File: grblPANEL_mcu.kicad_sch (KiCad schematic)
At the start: 28 parts, among them J201 2x5x1.27mm, J202 USB_C_Receptacle_USB2.0, SW201 SW_Push, SW202 SW_Push, U201 STM32G0B1CxTxN, U202 USBLC6-2SC6, Y201 8MHz

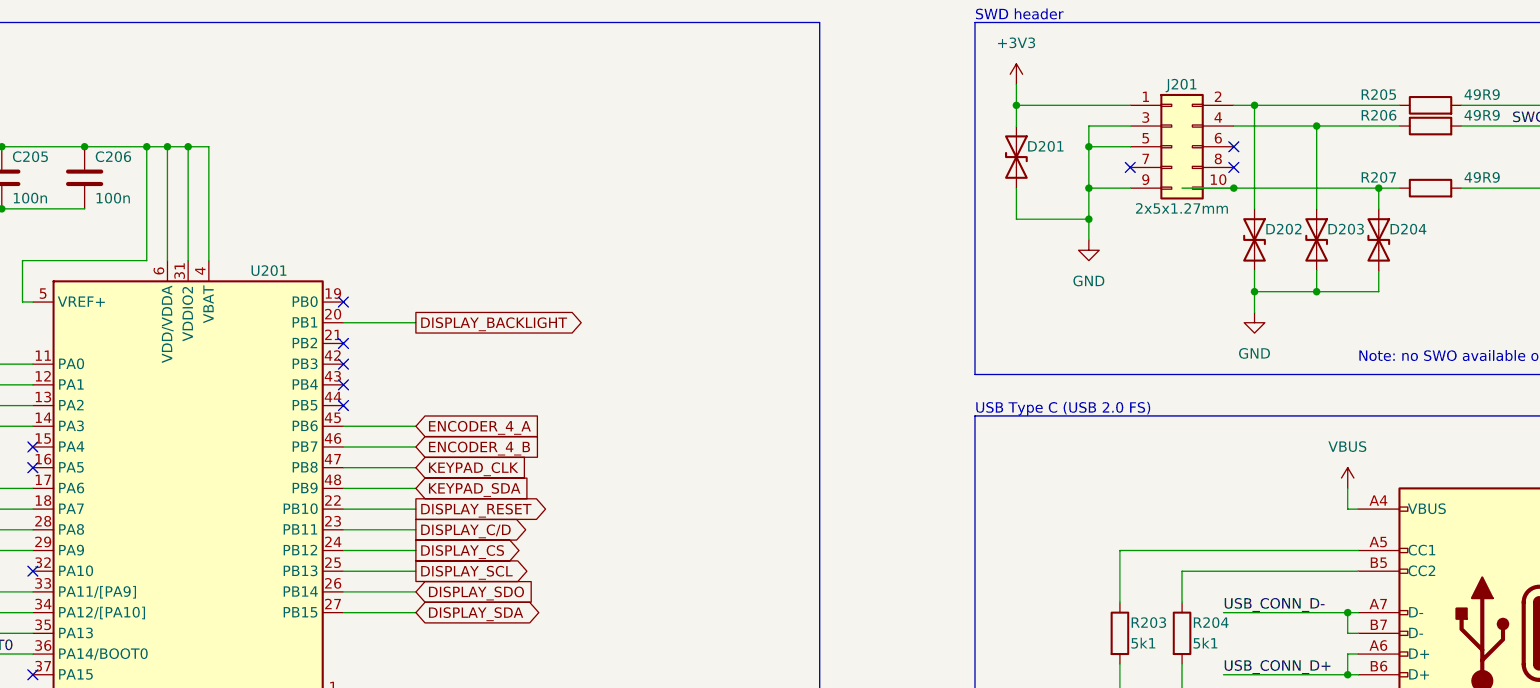
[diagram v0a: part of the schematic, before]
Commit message: ERC fixes
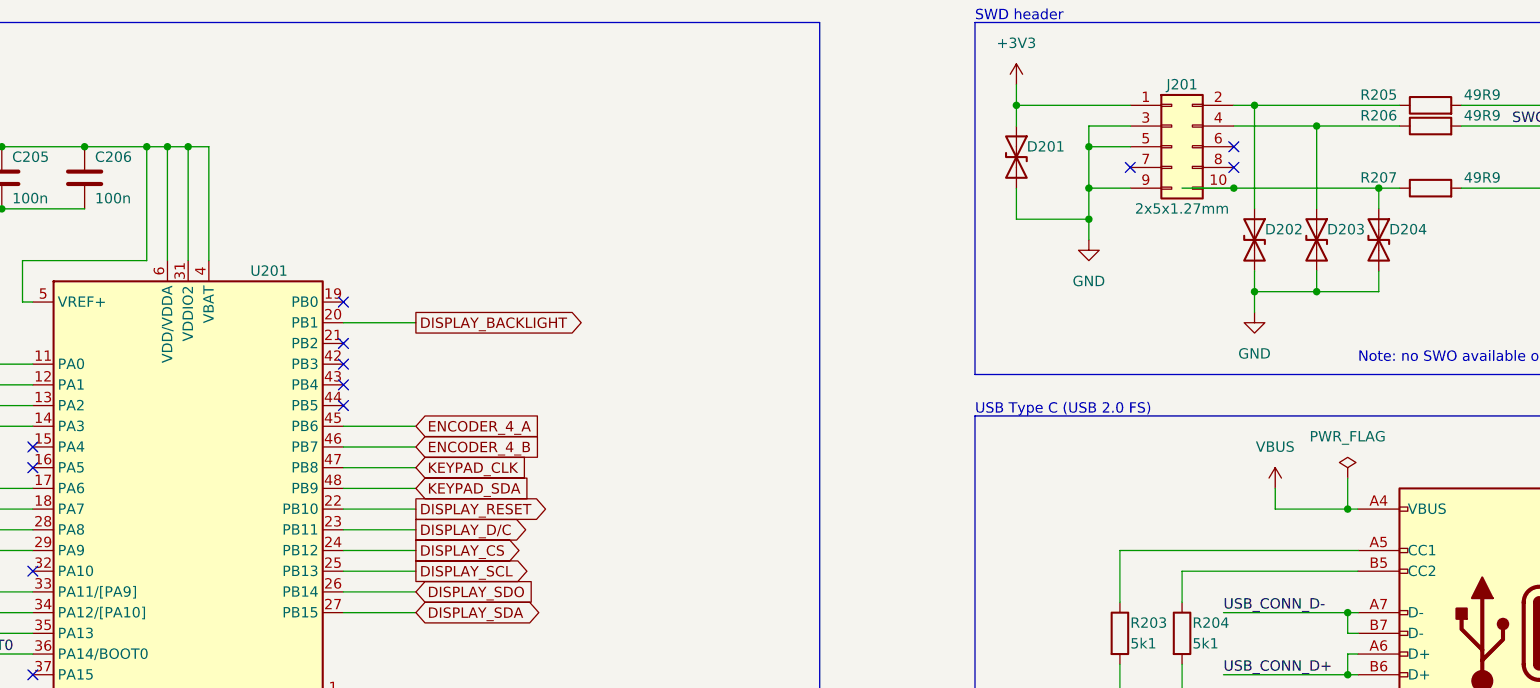
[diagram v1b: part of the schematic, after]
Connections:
- net DISPLAY_C/D renamed DISPLAY_D/C

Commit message: Refresh
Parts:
- removed C202: 1u, symbol Device:C
- removed C203, C206: 100n, symbol Device:C
- added C204: 100n, Capacitor_SMD:C_0603_1608Metric, symbol Device:C
- added R201, R203, R204: 0, Resistor_SMD:R_0603_1608Metric, symbol Device:R
- C201: footprint (none) -> Capacitor_SMD:C_0805_2012Metric
- C202: renamed from C204; footprint (none) -> Capacitor_SMD:C_0603_1608Metric
- C203: renamed from C205; footprint (none) -> Capacitor_SMD:C_0603_1608Metric
- C205: renamed from C207; footprint (none) -> Capacitor_SMD:C_0603_1608Metric
- C206: renamed from C208; footprint (none) -> Capacitor_SMD:C_0603_1608Metric
- C207: renamed from C209; footprint (none) -> Capacitor_SMD:C_0603_1608Metric
- C208: renamed from C210; footprint (none) -> Capacitor_SMD:C_0603_1608Metric
- D201, D202, D203, D204: footprint (none) -> Diode_SMD:D_SOD-323
- J201: footprint (none) -> dresco:FTSH-105-01-L-DV-K
- J202: footprint (none) -> Connector_USB:USB_C_Receptacle_HRO_TYPE-C-31-M-12
- R202: renamed from R201; value 300 -> 200; footprint (none) -> Resistor_SMD:R_0603_1608Metric
- R205: renamed from R202; footprint (none) -> Resistor_SMD:R_0603_1608Metric
- R206: renamed from R203; footprint (none) -> Resistor_SMD:R_0603_1608Metric
- R207: renamed from R204; footprint (none) -> Resistor_SMD:R_0603_1608Metric
- R208: renamed from R205; footprint (none) -> Resistor_SMD:R_0603_1608Metric
- R209: renamed from R206; footprint (none) -> Resistor_SMD:R_0603_1608Metric
- R210: renamed from R207; footprint (none) -> Resistor_SMD:R_0603_1608Metric
- SW201, SW202: footprint (none) -> Connector_Pin:Pin_D1.0mm_L10.0mm_LooseFit
- Y201: footprint (none) -> Crystal:Crystal_SMD_3225-4Pin_3.2x2.5mm
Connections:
- net +3V3: now also R204.2; no longer U201.31 (VDDIO2), U201.5 (VREF+)
- net GND: now also C204.2, R201.1, R203.2; no longer U201.30 (VSS)
- new net: C204.1, R204.1, U201.31 (VDDIO2)
- new net: R203.1, U201.30 (VSS)
- new net: R201.2, U201.5 (VREF+)
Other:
- note added: "Note: May source either STM32G0B1CET (general purpose) or STM32G0B1CETxN (power delivery) MCU parts, depending on availability. Note the following difference in pinouts; Pin GP PD 30 PC6 VSS 31 PC7 VDDIO2 Optional connection to power rails through 0 ohm resistors."
- note removed: "Note: May source either STM32G0B1CET (general purpose) or STM32G0B1CETxN (power delivery) MCU parts, depending on availability. Note the following difference in pinouts; Pin GP PD 30 PC6 VSS 31 PC7 VDDIO2 Either produce PD specific board rev, or connect to power rails through 0 ohm resistors?"
- moved on the sheet: C201, C202, C203, D203, D204

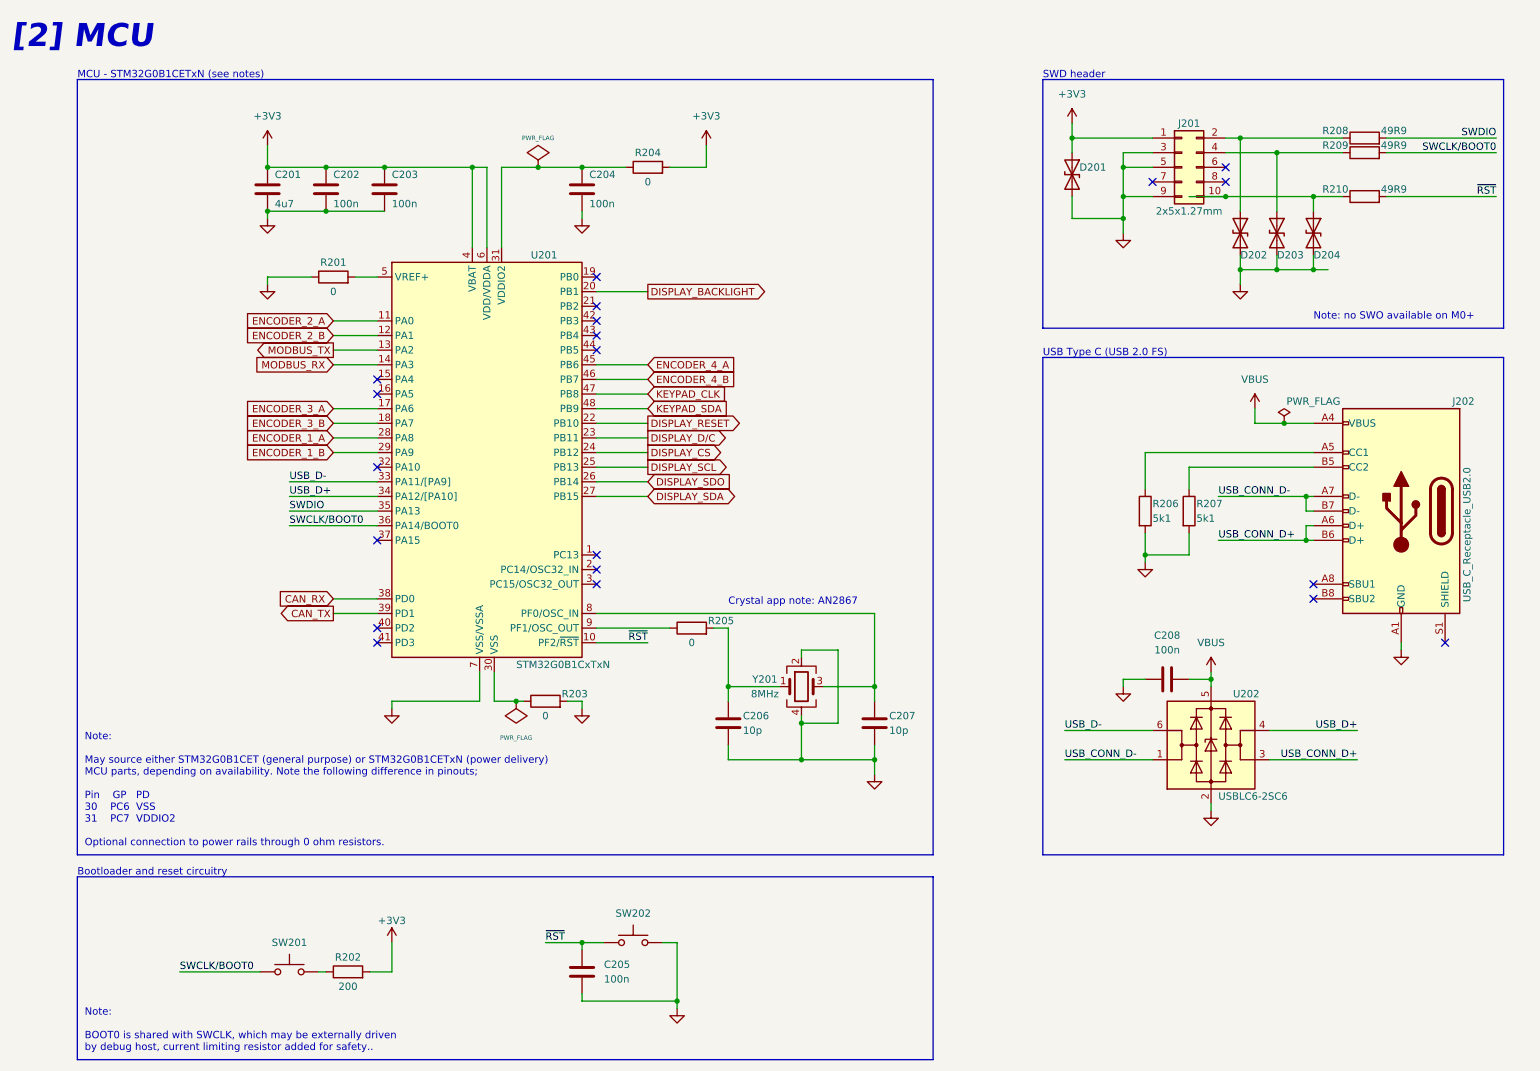
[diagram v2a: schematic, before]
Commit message: Status LED & annotation cleanup
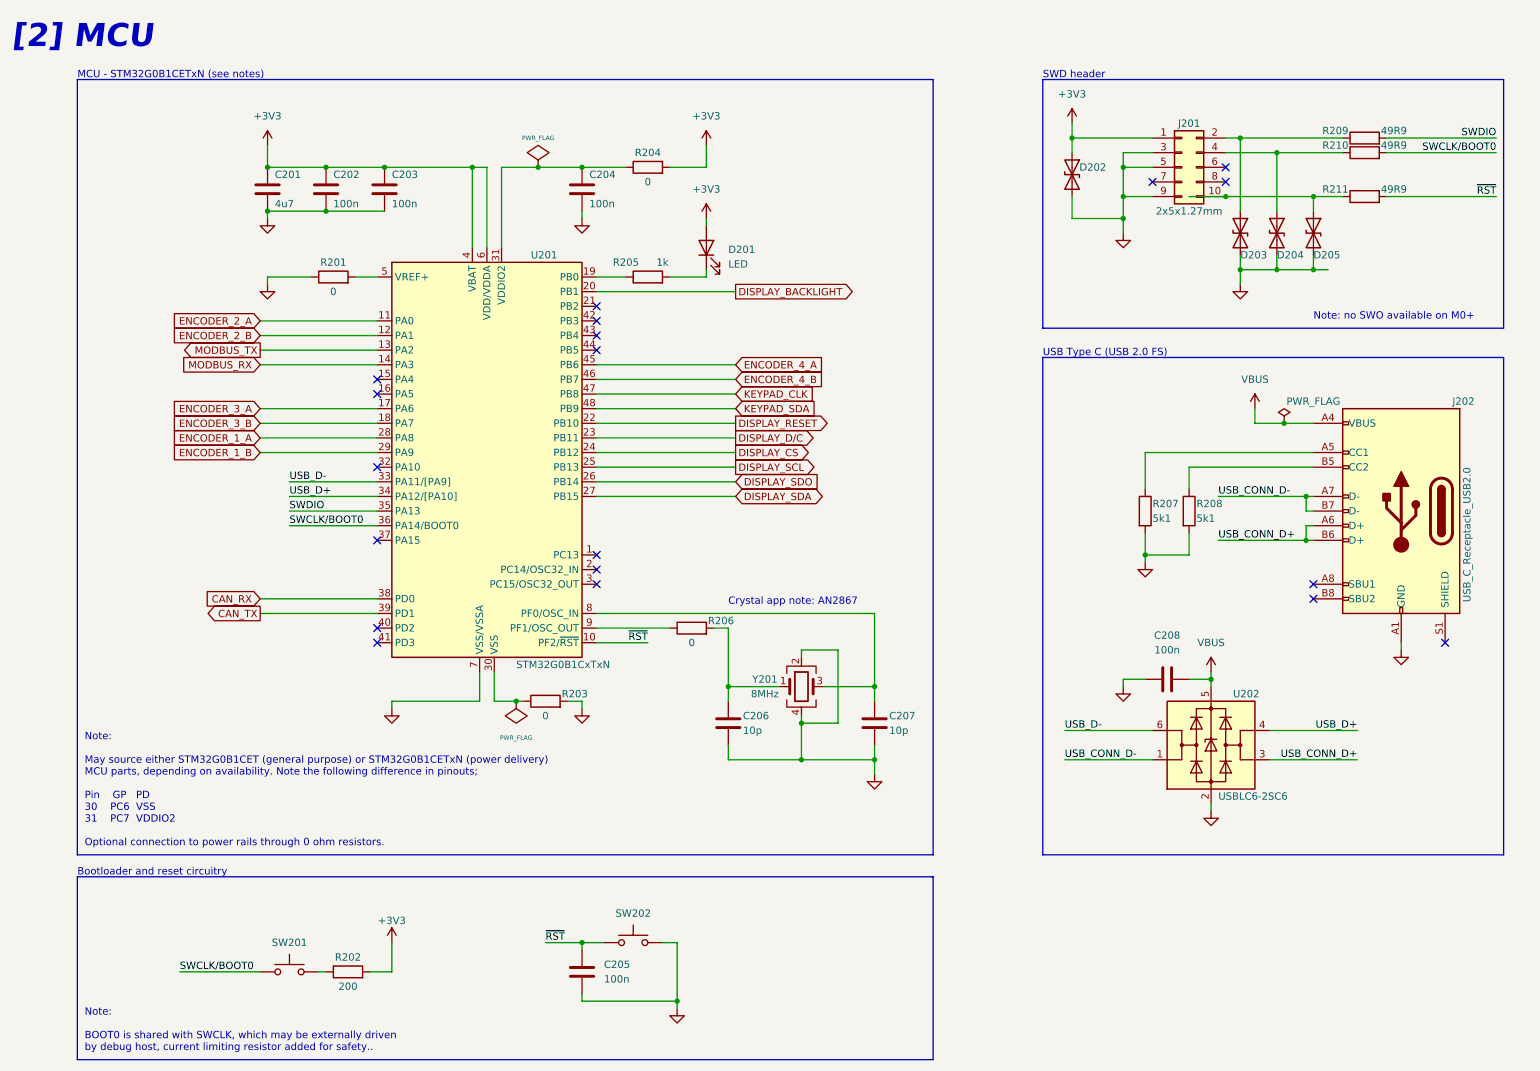
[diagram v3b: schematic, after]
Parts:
- added D201: LED, LED_SMD:LED_0603_1608Metric, symbol Device:LED
- added R205: 1k, Resistor_SMD:R_0603_1608Metric, symbol Device:R
- renumbered D201 to D202, D202 to D203, D203 to D204, D204 to D205, R205 to R206, R206 to R207, R207 to R208, R208 to R209, R209 to R210, R210 to R211
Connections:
- net +3V3: now also D201.2 (A)
- net at U201.19 (PB0): now also R205.1
- new net: D201.1 (K), R205.2
- no-connect marks 20 -> 19

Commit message: Weeny schematic update
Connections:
- net USB_CONN_CC1: now reaches J202.A5 (CC1), R207.1
- net USB_CONN_CC2: now reaches J202.B5 (CC2), R208.1
- net HSE_IN: now reaches C207.1, U201.8 (PF0/OSC_IN), Y201.3
- net XTAL_IN: now reaches C206.1, R206.2, Y201.1
- net HSE_OUT: now reaches R206.1, U201.9 (PF1/OSC_OUT)
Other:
- note added: "Cl1=Cl2=2*(C0-Cs)"
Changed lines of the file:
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@@
+    (effects (font (size 1.27 1.27)) (justify left bottom))
+  )
+  (text "Cl1=Cl2=2*(C0-Cs)" (at 142.24 147.32 0)
     (effects (font (size 1.27 1.27)) (justify left bottom))
   )
@@
     (effects (font (size 1.27 1.27)) (justify right bottom))
   )
+  (label "XTAL_IN" (at 139.7 132.08 0)
+    (effects (font (size 1.27 1.27)) (justify left bottom))
+  )
   (label "USB_D-" (at 63.5 96.52 0)
     (effects (font (size 1.27 1.27)) (justify left bottom))
   )
+  (label "HSE_IN" (at 125.73 119.38 180)
+    (effects (font (size 1.27 1.27)) (justify right bottom))
+  )
   (label "USB_CONN_D-" (at 224.79 99.06 0)
     (effects (font (size 1.27 1.27)) (justify left bottom))
   )
+  (label "USB_CONN_CC2" (at 224.79 93.98 0)
+    (effects (font (size 1.27 1.27)) (justify left bottom))
+  )
   (label "USB_CONN_D+" (at 248.92 144.78 180)
     (effects (font (size 1.27 1.27)) (justify right bottom))
@@
     (effects (font (size 1.27 1.27)) (justify left bottom))
   )
+  (label "USB_CONN_CC1" (at 224.79 91.44 0)
+    (effects (font (size 1.27 1.27)) (justify left bottom))
+  )
   (label "USB_CONN_D-" (at 198.12 144.78 0)
     (effects (font (size 1.27 1.27)) (justify left bottom))
@@
   (label "SWCLK{slash}BOOT0" (at 44.45 181.61 0)
     (effects (font (size 1.27 1.27)) (justify left bottom))
+  )
+  (label "HSE_OUT" (at 125.73 121.92 180)
+    (effects (font (size 1.27 1.27)) (justify right bottom))
   )
   (label "~{RST}" (at 273.05 46.99 180)
@@
   (symbol (lib_id "Device:Crystal_GND24") (at 152.4 132.08 0) (unit 1)
     (in_bom yes) (on_board yes)
-    (property "Reference" "Y201" (id 0) (at 146.05 130.81 0))
-    (property "Value" "8MHz" (id 1) (at 146.05 133.35 0))
+    (property "Reference" "Y201" (id 0) (at 147.32 129.54 0))
+    (property "Value" "8MHz" (id 1) (at 147.32 133.35 0))
     (property "Footprint" "Crystal:Crystal_SMD_3225-4Pin_3.2x2.5mm" (id 2) (at 152.4 132.08 0)
       (effects (font (size 1.27 1.27)) hide)
